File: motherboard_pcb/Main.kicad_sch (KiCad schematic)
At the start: 24 parts

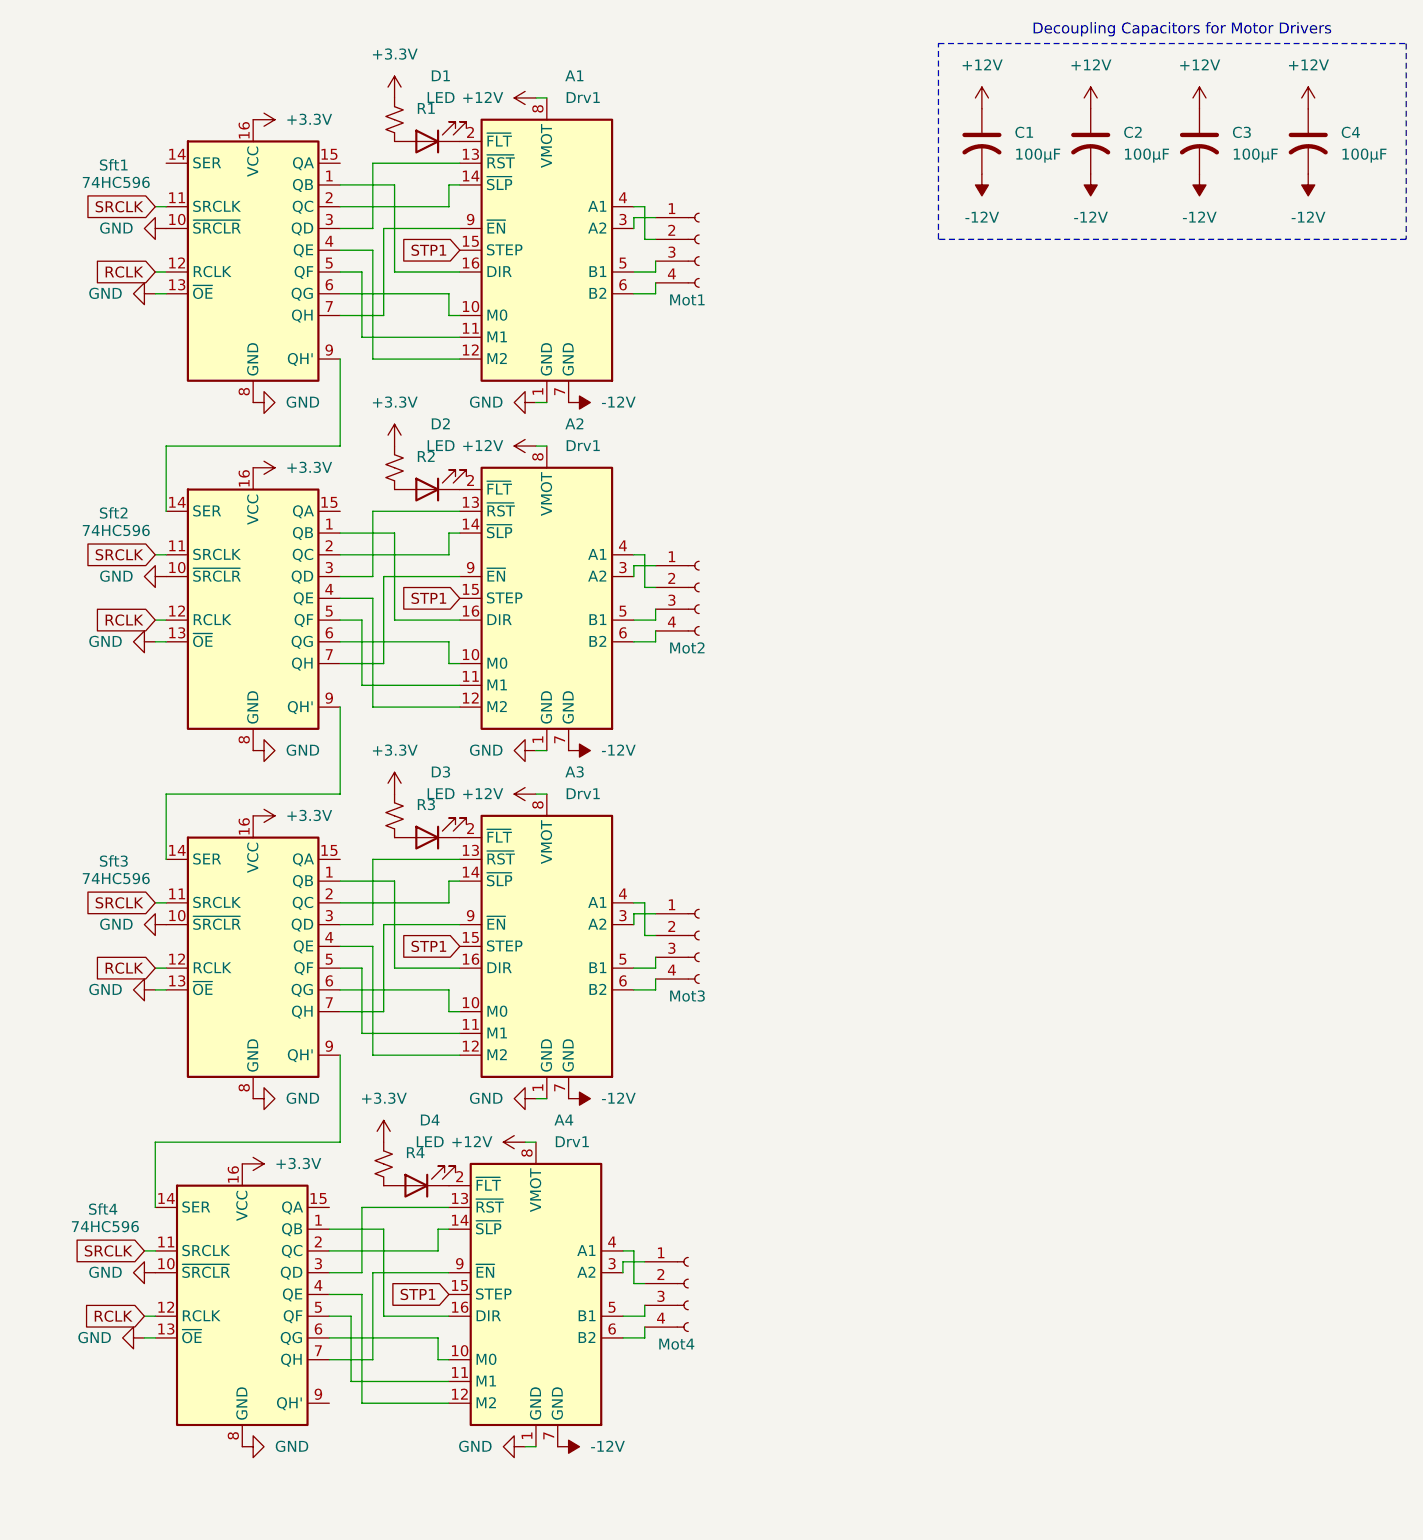
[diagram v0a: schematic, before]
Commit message: Most of the motor stuff has been routed
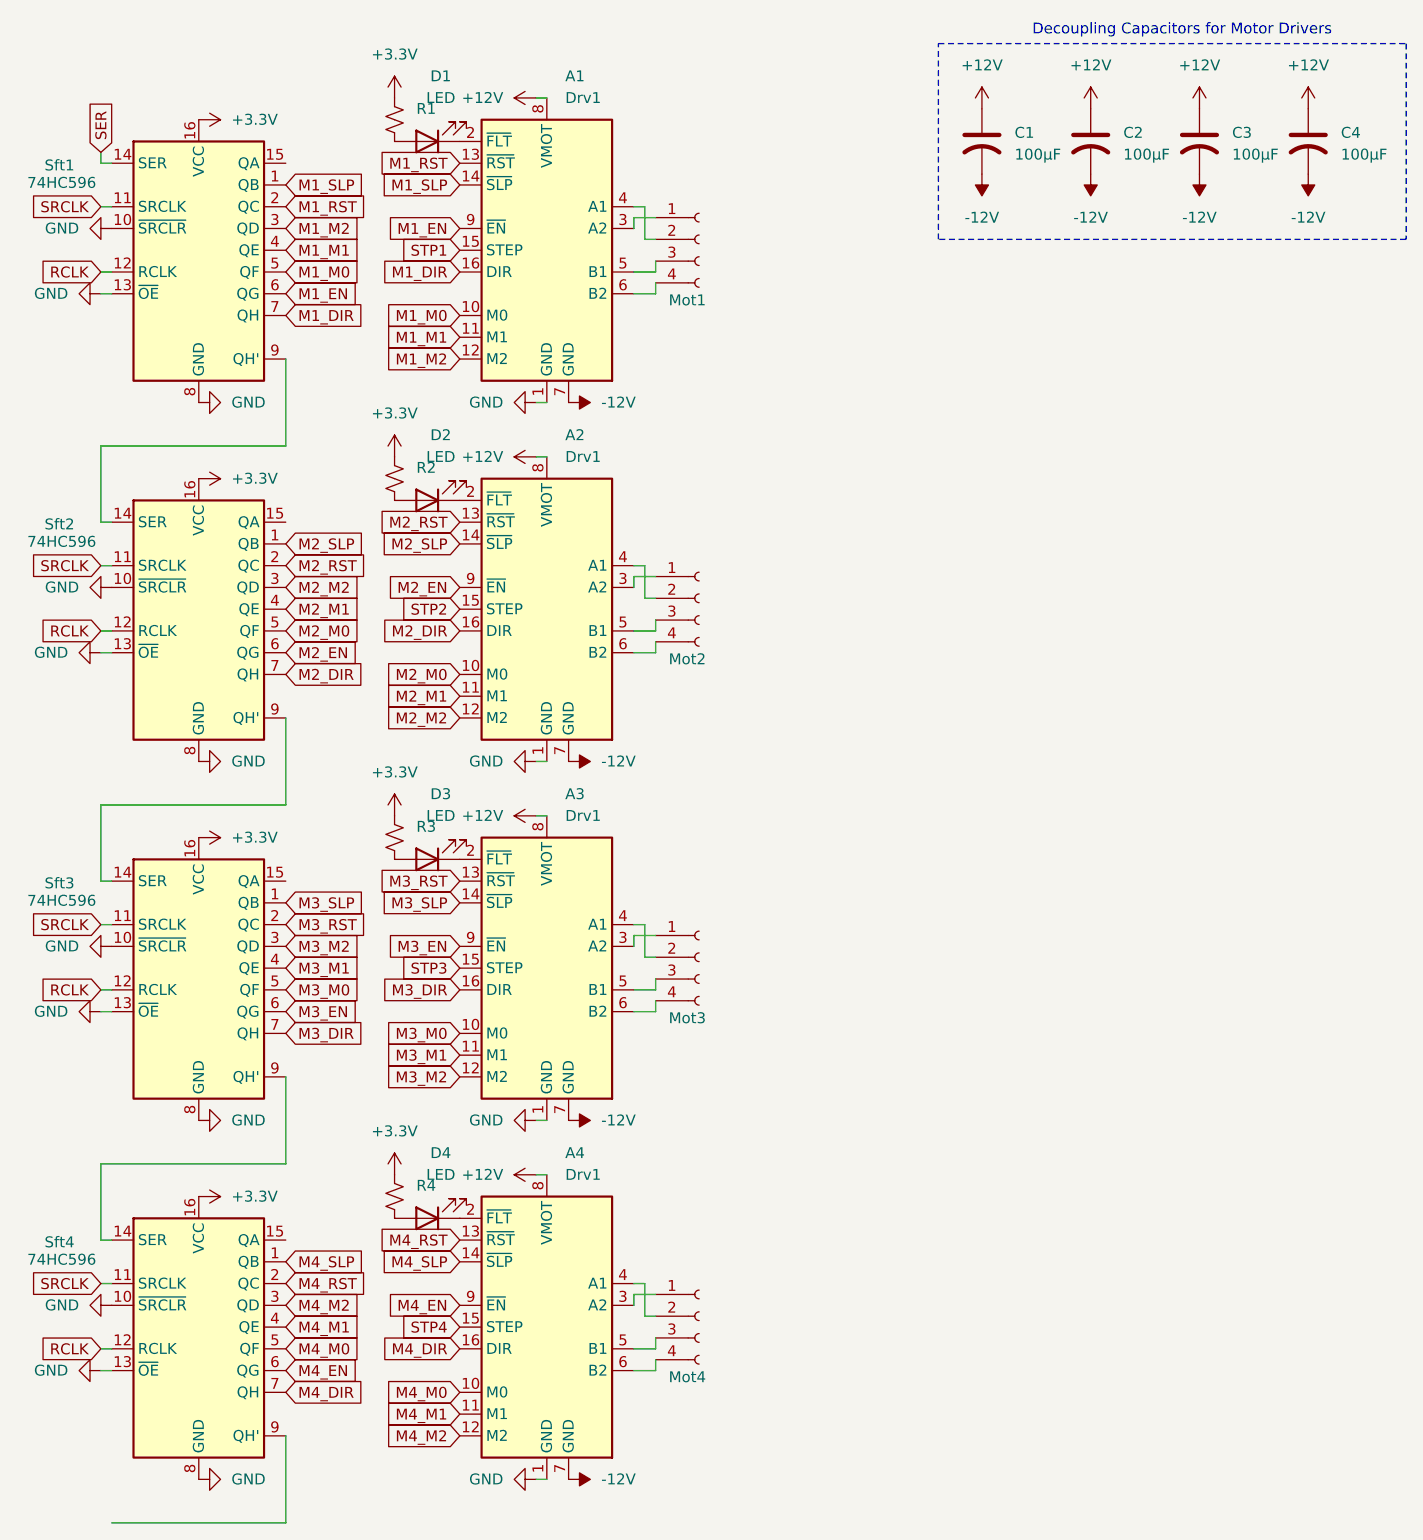
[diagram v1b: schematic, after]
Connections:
- net STP1: no longer A2.15 (STEP), A3.15 (STEP), A4.15 (STEP)
- net M4_DIR: now reaches A4.16 (DIR)
- net M4_DIR: now also Sft4.7 (QH); no longer Sft4.1 (QB)
- net M4_RST: now reaches Sft4.2 (QC)
- net M4_RST: now also A4.13 (~{RST}); no longer A4.14 (~{SLP})
- net M4_M2: now reaches Sft4.3 (QD)
- net M4_M2: now also A4.12 (M2); no longer A4.13 (~{RST})
- net M4_M1: now reaches Sft4.4 (QE)
- net M4_M1: now also A4.11 (M1); no longer A4.12 (M2)
- net M4_M0: now reaches Sft4.5 (QF)
- net M4_M0: now also A4.10 (M0); no longer A4.11 (M1)
- net M4_EN: now reaches Sft4.6 (QG)
- net M4_EN: now also A4.9 (~{EN}); no longer A4.10 (M0)
- net M2_DIR: now reaches A2.16 (DIR)
- net M2_DIR: now also Sft2.7 (QH); no longer Sft2.1 (QB)
- net M2_RST: now reaches Sft2.2 (QC)
- net M2_RST: now also A2.13 (~{RST}); no longer A2.14 (~{SLP})
- net M2_M2: now reaches Sft2.3 (QD)
- net M2_M2: now also A2.12 (M2); no longer A2.13 (~{RST})
- net M2_M1: now reaches Sft2.4 (QE)
- net M2_M1: now also A2.11 (M1); no longer A2.12 (M2)
- net M2_M0: now reaches Sft2.5 (QF)
- net M2_M0: now also A2.10 (M0); no longer A2.11 (M1)
- net M2_EN: now reaches Sft2.6 (QG)
- net M2_EN: now also A2.9 (~{EN}); no longer A2.10 (M0)
- net M1_DIR: now reaches A1.16 (DIR)
- net M1_DIR: now also Sft1.7 (QH); no longer Sft1.1 (QB)
- net SER: now reaches Sft1.14 (SER)
- net M1_RST: now reaches Sft1.2 (QC)
- net M1_RST: now also A1.13 (~{RST}); no longer A1.14 (~{SLP})
- net M1_M2: now reaches Sft1.3 (QD)
- net M1_M2: now also A1.12 (M2); no longer A1.13 (~{RST})
- net M1_M1: now reaches Sft1.4 (QE)
- net M1_M1: now also A1.11 (M1); no longer A1.12 (M2)
- net M1_M0: now reaches Sft1.5 (QF)
- net M1_M0: now also A1.10 (M0); no longer A1.11 (M1)
- net M1_EN: now reaches Sft1.6 (QG)
- net M1_EN: now also A1.9 (~{EN}); no longer A1.10 (M0)
- net M3_DIR: now reaches A3.16 (DIR)
- net M3_DIR: now also Sft3.7 (QH); no longer Sft3.1 (QB)
- net M3_RST: now reaches Sft3.2 (QC)
- net M3_RST: now also A3.13 (~{RST}); no longer A3.14 (~{SLP})
- net M3_M2: now reaches Sft3.3 (QD)
- net M3_M2: now also A3.12 (M2); no longer A3.13 (~{RST})
- net M3_M1: now reaches Sft3.4 (QE)
- net M3_M1: now also A3.11 (M1); no longer A3.12 (M2)
- net M3_M0: now reaches Sft3.5 (QF)
- net M3_M0: now also A3.10 (M0); no longer A3.11 (M1)
- net M3_EN: now reaches Sft3.6 (QG)
- net M3_EN: now also A3.9 (~{EN}); no longer A3.10 (M0)
- new net M1_SLP: A1.14 (~{SLP}), Sft1.1 (QB)
- new net M2_SLP: A2.14 (~{SLP}), Sft2.1 (QB)
- new net M3_SLP: A3.14 (~{SLP}), Sft3.1 (QB)
- new net M4_SLP: A4.14 (~{SLP}), Sft4.1 (QB)
- new net STP2: A2.15 (STEP)
- new net STP3: A3.15 (STEP)
- new net STP4: A4.15 (STEP)
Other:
- moved on the sheet: Sft1

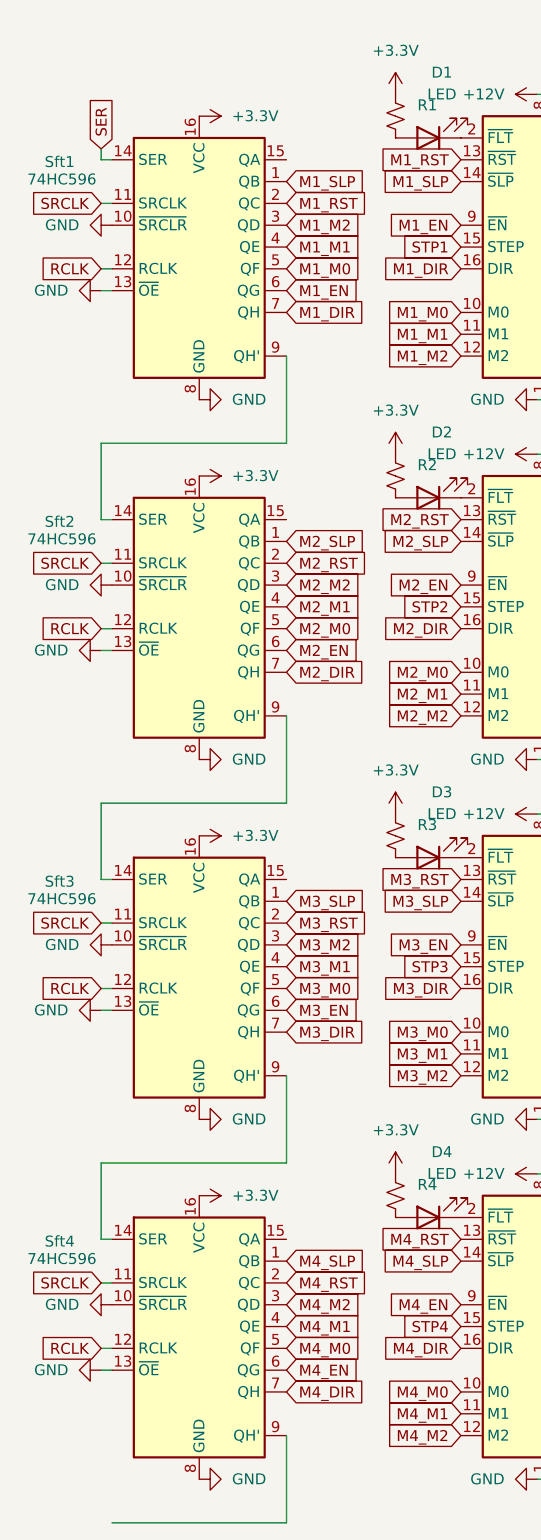
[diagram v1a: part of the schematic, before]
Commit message: Routed all connections to shift registers
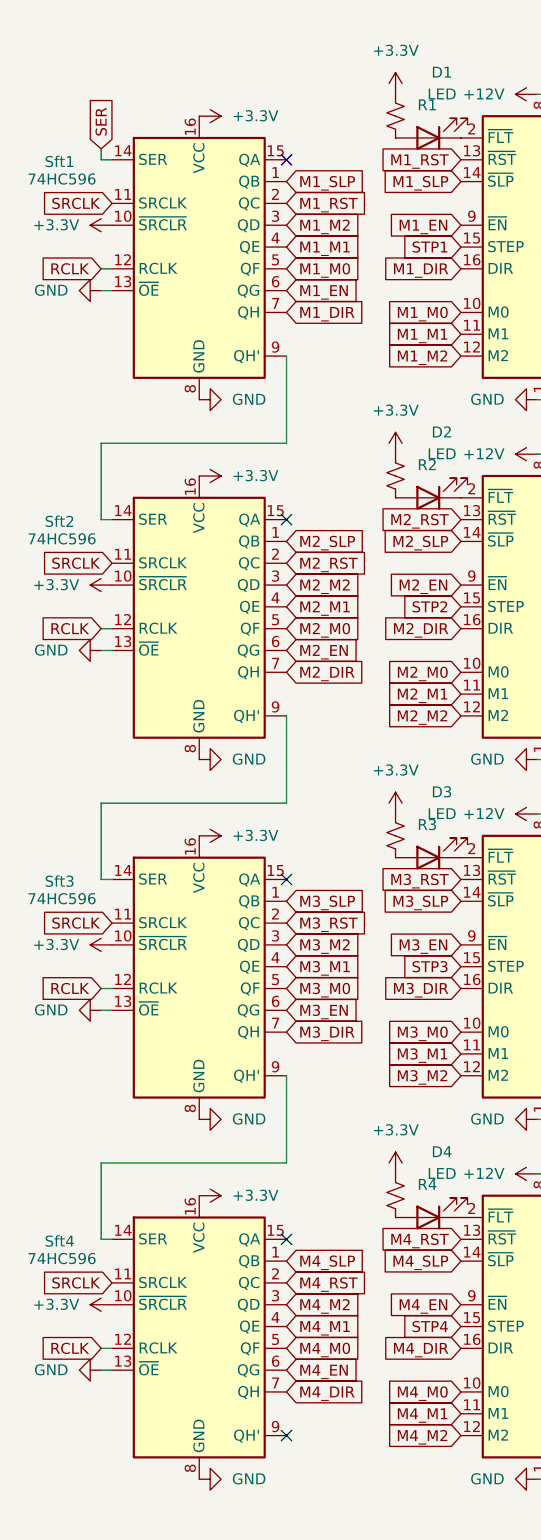
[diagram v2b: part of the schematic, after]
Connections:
- net +3.3V: now also Sft1.10 (~{SRCLR}), Sft2.10 (~{SRCLR}), Sft3.10 (~{SRCLR}), Sft4.10 (~{SRCLR})
- net GND: no longer Sft1.10 (~{SRCLR}), Sft2.10 (~{SRCLR}), Sft3.10 (~{SRCLR}), Sft4.10 (~{SRCLR})
- no-connect marks 0 -> 5
